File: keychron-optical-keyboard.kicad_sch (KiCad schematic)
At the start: 188 parts

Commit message: Add footprints
M  .gitignore
A  Footprints.pretty/BlackPill_STLINK.kicad_mod
M  Footprints.pretty/BlackPill_STLINK2.kicad_mod
M  Footprints.pretty/Keychron_Optical_Switch_1.25u.kicad_mod
M  Footprints.pretty/Keychron_Optical_Switch_1.5u.kicad_mod
M  Footprints.pretty/Keychron_Optical_Switch_1.75u.kicad_mod
M  Footprints.pretty/Keychron_Optical_Switch_1u.kicad_mod
M  Footprints.pretty/Keychron_Optical_Switch_2u.kicad_mod
M  MySymbols.kicad_sym
D  keychron-optical-keyboard-backups/keychron-optical-keyboard-2022-08-03_201538.zip
D  keychron-optical-keyboard-backups/keychron-optical-keyboard-2022-08-03_202112.zip
M  keychron-optical-keyboard.kicad_pcb
M  keychron-optical-keyboard.kicad_prl
M  keychron-optical-keyboard.kicad_sch
A  placek.py
A  resources/keychronpic.png
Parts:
- removed R? (x15): R, symbol Device:R
- added RP1, RP10, RP11, RP12, RP13, RP14, RP15, RP2, RP3, RP4, RP5, RP6, RP7, RP8, RP9: R_PT, Resistor_SMD:R_0805_2012Metric_Pad1.20x1.40mm_HandSolder, symbol MySymbols:R_PT
- H1, H10, H11, H12, H13, H14, H15, H16, H2, H3, H4, H5, H6, H7, H8, H9: renamed from H?; footprint (none) -> MyFootprints:MountingHole_2.2mm_M2_jlcpcb
- H17, H18, H19, H20: renamed from H?; footprint (none) -> MyFootprints:MountingHole_1.2mm_M1
- RL1, RL10, RL11, RL12, RL13, RL14, RL15, RL16, RL17, RL18, RL19, RL2, RL20, RL21, RL22, RL23, RL24, RL25, RL26, RL27, RL28, RL29, RL3, RL30, RL31, RL32, RL33, RL34, RL35, RL36, RL37, RL38, RL39, RL4, RL40, RL41, RL42, RL43, RL44, RL45, RL46, RL47, RL48, RL49, RL5, RL50, RL51, RL52, RL53, RL54, RL55, RL56, RL57, RL58, RL59, RL6, RL60, RL61, RL62, RL63, RL64, RL65, RL66, RL67, RL68, RL69, RL7, RL70, RL71, RL72, RL73, RL74, RL75, RL8, RL9: renamed from RL?; footprint (none) -> Resistor_SMD:R_1206_3216Metric_Pad1.30x1.75mm_HandSolder
- S1, S10, S11, S12, S13, S14, S15, S17, S18, S19, S2, S20, S21, S22, S23, S24, S25, S26, S27, S28, S3, S30, S31, S33, S34, S35, S36, S37, S38, S39, S4, S40, S41, S42, S43, S45, S47, S48, S49, S5, S50, S51, S52, S53, S54, S55, S56, S57, S59, S6, S60, S61, S62, S63, S64, S65, S67, S69, S7, S70, S71, S72, S73, S74, S75, S8, S9: renamed from Q?; footprint (none) -> MyFootprints:Keychron_Optical_Switch_1u
- S16, S29: renamed from Q?; footprint (none) -> MyFootprints:Keychron_Optical_Switch_1.5u
- S32, S58: renamed from Q?; footprint (none) -> MyFootprints:Keychron_Optical_Switch_1.25u
- S44, S46, S66, S68: renamed from Q?; footprint (none) -> MyFootprints:Keychron_Optical_Switch_1.75u
- U1: renamed from U?; footprint blackpill:BlackPill_STLINK -> MyFootprints:BlackPill_STLINK2
- gave numbers to parts that had none: 2
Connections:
- net 3v3: now also RP1.2, RP10.2, RP11.2, RP12.2, RP13.2, RP14.2, RP15.2, RP2.2, RP3.2, RP4.2, RP5.2, RP6.2, RP7.2, RP8.2, RP9.2
- net col1: now also RP1.1
- net col10: now also RP10.1
- net col11: now also RP11.1
- net col12: now also RP12.1
- net col13: now also RP13.1
- net col14: now also RP14.1
- net col15: now also RP15.1
- net col2: now also RP2.1
- net col3: now also RP3.1
- net col4: now also RP4.1
- net col5: now also RP5.1
- net col6: now also RP6.1
- net col7: now also RP7.1
- net col8: now also RP8.1
- net col9: now also RP9.1

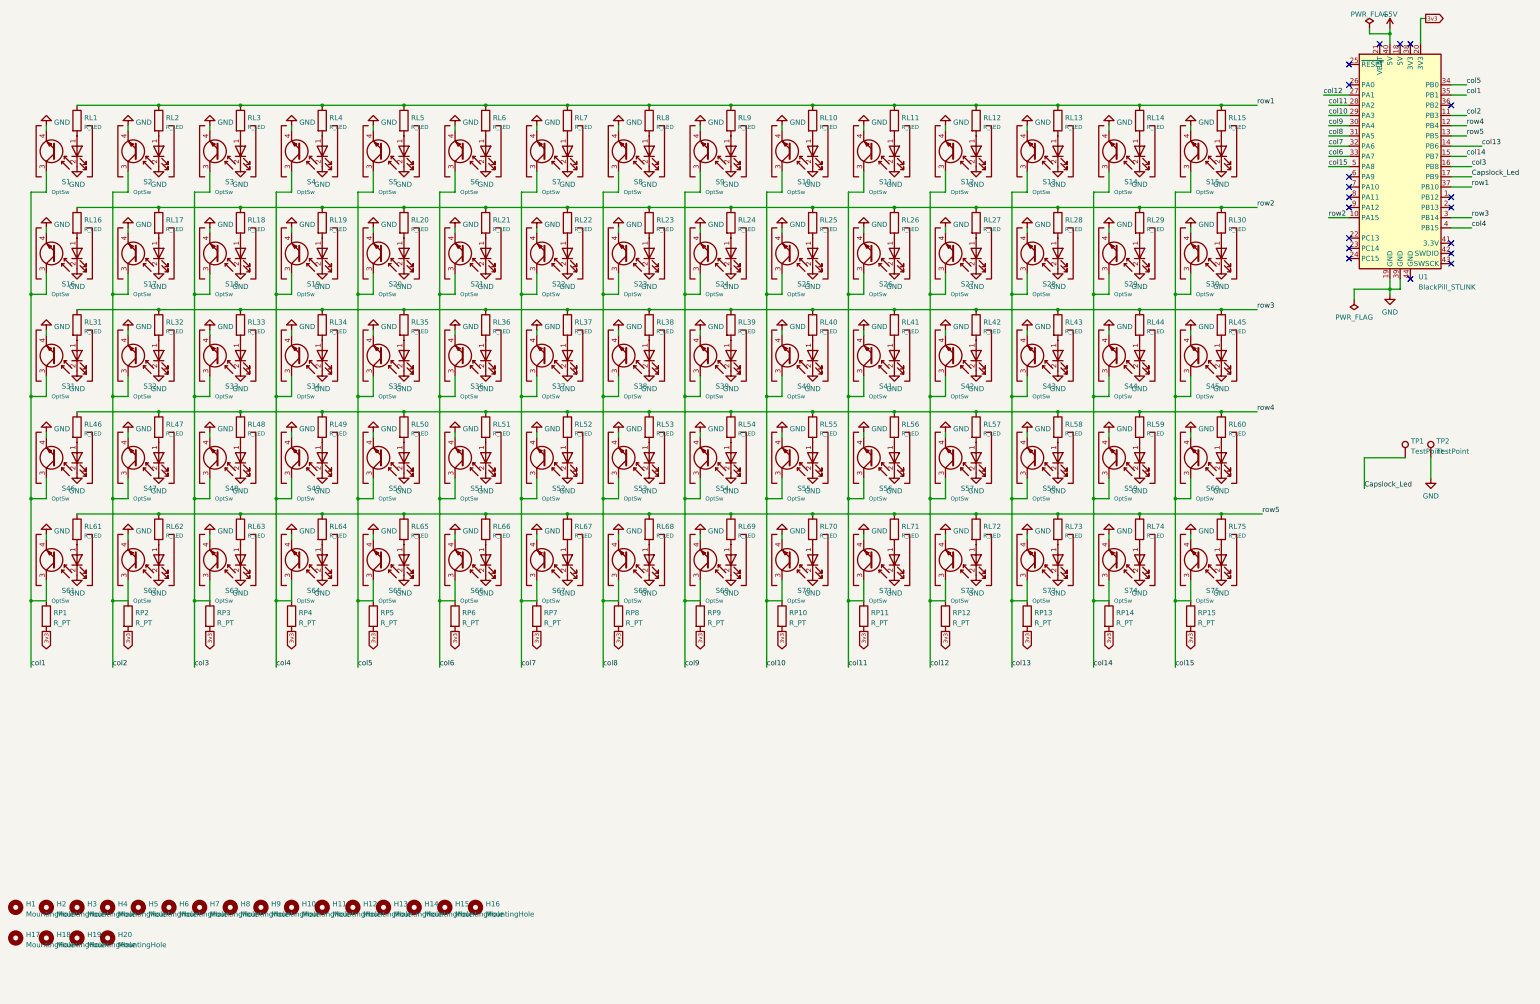
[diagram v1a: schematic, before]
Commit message: Route tracks, add switch plate, scripts
Add python scripts to route tracks, draw border, place footprints

A  Footprints.pretty/BlackPill_STLINK_Down.kicad_mod
A  Footprints.pretty/Border_PCB_WR.kicad_mod
M  Footprints.pretty/Keychron_Optical_Switch_1.25u.kicad_mod
M  Footprints.pretty/Keychron_Optical_Switch_1.5u.kicad_mod
D  Footprints.pretty/Keychron_Optical_Switch_1.75u.kicad_mod
M  Footprints.pretty/Keychron_Optical_Switch_1u.kicad_mod
D  Footprints.pretty/Keychron_Optical_Switch_2u.kicad_mod
A  Footprints.pretty/MountingHole_2.2mm_M2_ISO7380_Pad.kicad_mod
A  Footprints.pretty/SMTSO_M1.6.kicad_mod
A  Footprints.pretty/SMTSO_M2.kicad_mod
M  Footprints.pretty/Switch_Cutout.kicad_mod
M  MySymbols.kicad_sym
D  keychron-optical-keyboard-backups/keychron-optical-keyboard-2022-08-03_203051.zip
D  keychron-optical-keyboard-backups/keychron-optical-keyboard-2022-08-03_203709.zip
D  keychron-optical-keyboard-backups/keychron-optical-keyboard-2022-08-03_204429.zip
D  keychron-optical-keyboard-backups/keychron-optical-keyboard-2022-08-03_204938.zip
M  keychron-optical-keyboard.kicad_pcb
M  keychron-optical-keyboard.kicad_prl
M  keychron-optical-keyboard.kicad_sch
M  placek.py
A  resources/AL-S0602IRC-VI-12P9.pdf
A  resources/AL-S0602PTB-VI-1216.pdf
A  resources/IMG_0621.JPG
M  resources/keychronpic.png
A  switch-plate/.gitignore
A  switch-plate/fp-lib-table
A  switch-plate/switch-plate.kicad_pcb
A  switch-plate/switch-plate.kicad_prl
A  switch-plate/switch-plate.kicad_pro
A  switch-plate/switch-plate.kicad_sch
A  switch-plate/sym-lib-table
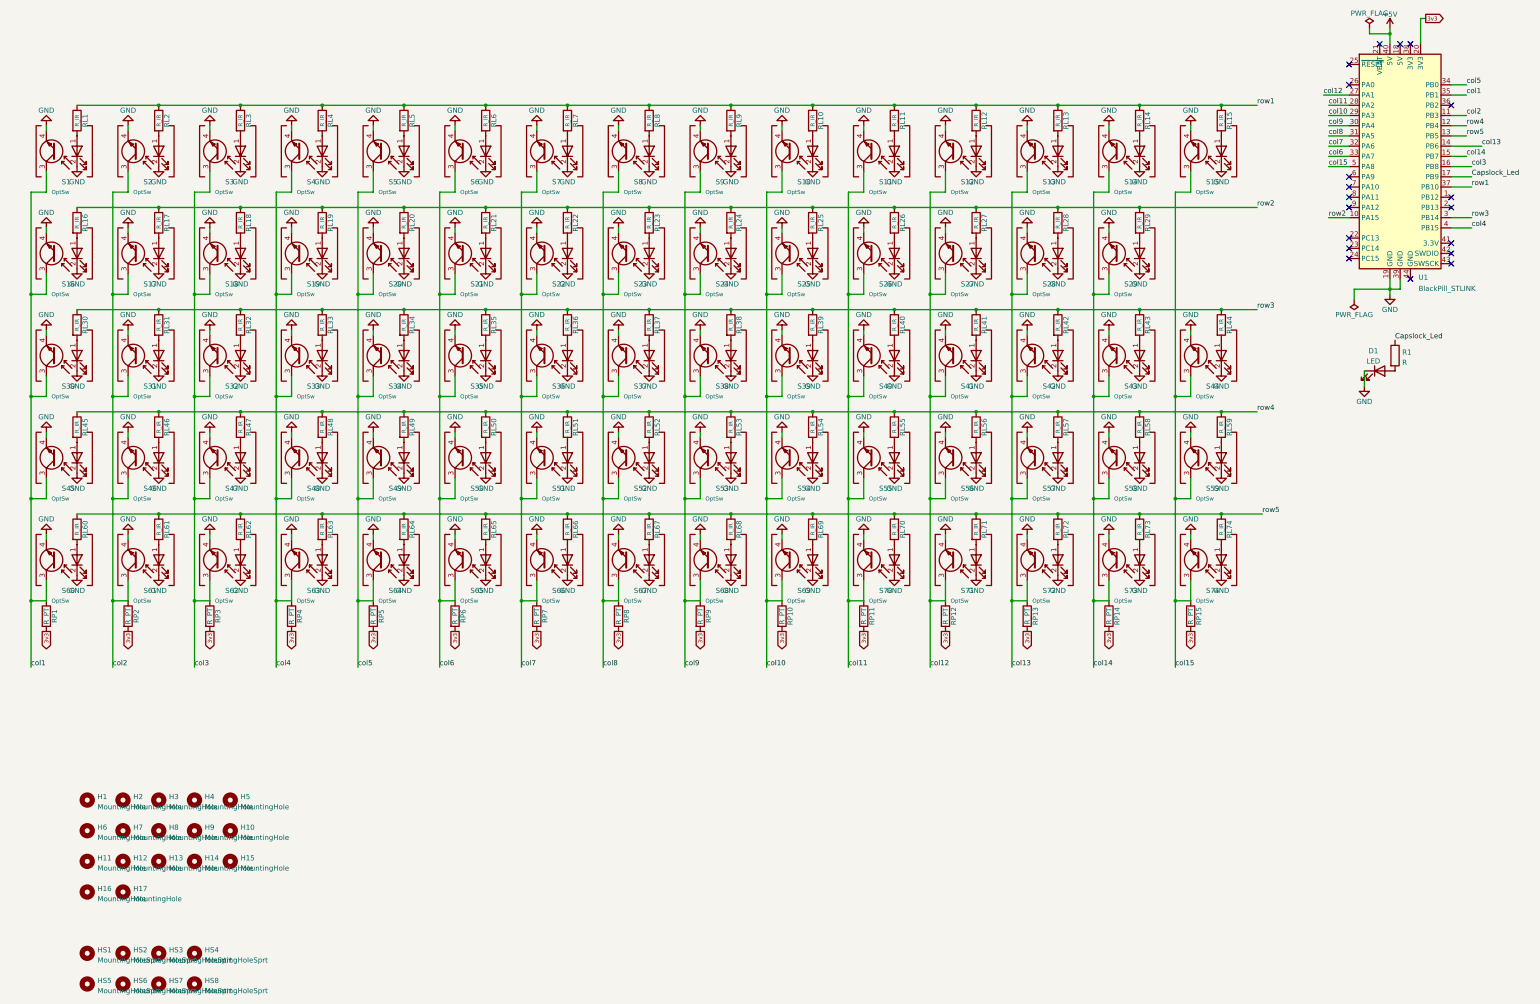
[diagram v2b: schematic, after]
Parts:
- removed H18, H19, H20: MountingHole, MyFootprints:MountingHole_1.2mm_M1, symbol Mechanical:MountingHole
- removed RL30: R_LED, Resistor_SMD:R_1206_3216Metric_Pad1.30x1.75mm_HandSolder, symbol MySymbols:R_LED
- removed S30: OptSw, MyFootprints:Keychron_Optical_Switch_1u, symbol MySymbols:OptSw
- removed TP1, TP2: TestPoint, TestPoint:TestPoint_THTPad_1.0x1.0mm_Drill0.5mm, symbol Connector:TestPoint
- added D1: LED, LED_SMD:LED_0603_1608Metric_Pad1.05x0.95mm_HandSolder, symbol Device:LED
- added HS1, HS2, HS3, HS4, HS5, HS6, HS7, HS8: MountingHoleSprt, MyFootprints:SMTSO_M2, symbol MySymbols:MountingHoleSprt
- added R1: R, Resistor_SMD:R_0805_2012Metric_Pad1.20x1.40mm_HandSolder, symbol Device:R
- H1, H10, H11, H12, H13, H14, H15, H16, H2, H3, H4, H5, H6, H7, H8, H9: footprint MyFootprints:MountingHole_2.2mm_M2_jlcpcb -> MyFootprints:SMTSO_M1.6
- H17: footprint MyFootprints:MountingHole_1.2mm_M1 -> MyFootprints:SMTSO_M1.6
- RL1: value R_LED -> R_IR; footprint Resistor_SMD:R_1206_3216Metric_Pad1.30x1.75mm_HandSolder -> Resistor_SMD:R_0805_2012Metric_Pad1.20x1.40mm_HandSolder; symbol MySymbols:R_LED -> MySymbols:R_IR; JLC 0603-1608 -> (none); LCSC C4190 -> (none)
- RL10, RL11, RL12, RL13, RL14, RL15, RL16, RL17, RL18, RL19, RL2, RL20, RL21, RL22, RL23, RL24, RL25, RL26, RL27, RL28, RL29, RL3, RL4, RL5, RL6, RL7, RL8, RL9: value R_LED -> R_IR; footprint Resistor_SMD:R_1206_3216Metric_Pad1.30x1.75mm_HandSolder -> Resistor_SMD:R_0805_2012Metric_Pad1.20x1.40mm_HandSolder; symbol MySymbols:R_LED -> MySymbols:R_IR
- RL30: renamed from RL31; value R_LED -> R_IR; footprint Resistor_SMD:R_1206_3216Metric_Pad1.30x1.75mm_HandSolder -> Resistor_SMD:R_0805_2012Metric_Pad1.20x1.40mm_HandSolder; symbol MySymbols:R_LED -> MySymbols:R_IR
- RL31: renamed from RL32; value R_LED -> R_IR; footprint Resistor_SMD:R_1206_3216Metric_Pad1.30x1.75mm_HandSolder -> Resistor_SMD:R_0805_2012Metric_Pad1.20x1.40mm_HandSolder; symbol MySymbols:R_LED -> MySymbols:R_IR
- RL32: renamed from RL33; value R_LED -> R_IR; footprint Resistor_SMD:R_1206_3216Metric_Pad1.30x1.75mm_HandSolder -> Resistor_SMD:R_0805_2012Metric_Pad1.20x1.40mm_HandSolder; symbol MySymbols:R_LED -> MySymbols:R_IR
- RL33: renamed from RL34; value R_LED -> R_IR; footprint Resistor_SMD:R_1206_3216Metric_Pad1.30x1.75mm_HandSolder -> Resistor_SMD:R_0805_2012Metric_Pad1.20x1.40mm_HandSolder; symbol MySymbols:R_LED -> MySymbols:R_IR
- RL34: renamed from RL35; value R_LED -> R_IR; footprint Resistor_SMD:R_1206_3216Metric_Pad1.30x1.75mm_HandSolder -> Resistor_SMD:R_0805_2012Metric_Pad1.20x1.40mm_HandSolder; symbol MySymbols:R_LED -> MySymbols:R_IR
- RL35: renamed from RL36; value R_LED -> R_IR; footprint Resistor_SMD:R_1206_3216Metric_Pad1.30x1.75mm_HandSolder -> Resistor_SMD:R_0805_2012Metric_Pad1.20x1.40mm_HandSolder; symbol MySymbols:R_LED -> MySymbols:R_IR
- RL36: renamed from RL37; value R_LED -> R_IR; footprint Resistor_SMD:R_1206_3216Metric_Pad1.30x1.75mm_HandSolder -> Resistor_SMD:R_0805_2012Metric_Pad1.20x1.40mm_HandSolder; symbol MySymbols:R_LED -> MySymbols:R_IR
- RL37: renamed from RL38; value R_LED -> R_IR; footprint Resistor_SMD:R_1206_3216Metric_Pad1.30x1.75mm_HandSolder -> Resistor_SMD:R_0805_2012Metric_Pad1.20x1.40mm_HandSolder; symbol MySymbols:R_LED -> MySymbols:R_IR
- RL38: renamed from RL39; value R_LED -> R_IR; footprint Resistor_SMD:R_1206_3216Metric_Pad1.30x1.75mm_HandSolder -> Resistor_SMD:R_0805_2012Metric_Pad1.20x1.40mm_HandSolder; symbol MySymbols:R_LED -> MySymbols:R_IR
- RL39: renamed from RL40; value R_LED -> R_IR; footprint Resistor_SMD:R_1206_3216Metric_Pad1.30x1.75mm_HandSolder -> Resistor_SMD:R_0805_2012Metric_Pad1.20x1.40mm_HandSolder; symbol MySymbols:R_LED -> MySymbols:R_IR
- RL40: renamed from RL41; value R_LED -> R_IR; footprint Resistor_SMD:R_1206_3216Metric_Pad1.30x1.75mm_HandSolder -> Resistor_SMD:R_0805_2012Metric_Pad1.20x1.40mm_HandSolder; symbol MySymbols:R_LED -> MySymbols:R_IR
- RL41: renamed from RL42; value R_LED -> R_IR; footprint Resistor_SMD:R_1206_3216Metric_Pad1.30x1.75mm_HandSolder -> Resistor_SMD:R_0805_2012Metric_Pad1.20x1.40mm_HandSolder; symbol MySymbols:R_LED -> MySymbols:R_IR
- RL42: renamed from RL43; value R_LED -> R_IR; footprint Resistor_SMD:R_1206_3216Metric_Pad1.30x1.75mm_HandSolder -> Resistor_SMD:R_0805_2012Metric_Pad1.20x1.40mm_HandSolder; symbol MySymbols:R_LED -> MySymbols:R_IR
- RL43: renamed from RL44; value R_LED -> R_IR; footprint Resistor_SMD:R_1206_3216Metric_Pad1.30x1.75mm_HandSolder -> Resistor_SMD:R_0805_2012Metric_Pad1.20x1.40mm_HandSolder; symbol MySymbols:R_LED -> MySymbols:R_IR
- RL44: renamed from RL45; value R_LED -> R_IR; footprint Resistor_SMD:R_1206_3216Metric_Pad1.30x1.75mm_HandSolder -> Resistor_SMD:R_0805_2012Metric_Pad1.20x1.40mm_HandSolder; symbol MySymbols:R_LED -> MySymbols:R_IR
- RL45: renamed from RL46; value R_LED -> R_IR; footprint Resistor_SMD:R_1206_3216Metric_Pad1.30x1.75mm_HandSolder -> Resistor_SMD:R_0805_2012Metric_Pad1.20x1.40mm_HandSolder; symbol MySymbols:R_LED -> MySymbols:R_IR
- RL46: renamed from RL47; value R_LED -> R_IR; footprint Resistor_SMD:R_1206_3216Metric_Pad1.30x1.75mm_HandSolder -> Resistor_SMD:R_0805_2012Metric_Pad1.20x1.40mm_HandSolder; symbol MySymbols:R_LED -> MySymbols:R_IR
- RL47: renamed from RL48; value R_LED -> R_IR; footprint Resistor_SMD:R_1206_3216Metric_Pad1.30x1.75mm_HandSolder -> Resistor_SMD:R_0805_2012Metric_Pad1.20x1.40mm_HandSolder; symbol MySymbols:R_LED -> MySymbols:R_IR
- RL48: renamed from RL49; value R_LED -> R_IR; footprint Resistor_SMD:R_1206_3216Metric_Pad1.30x1.75mm_HandSolder -> Resistor_SMD:R_0805_2012Metric_Pad1.20x1.40mm_HandSolder; symbol MySymbols:R_LED -> MySymbols:R_IR
- RL49: renamed from RL50; value R_LED -> R_IR; footprint Resistor_SMD:R_1206_3216Metric_Pad1.30x1.75mm_HandSolder -> Resistor_SMD:R_0805_2012Metric_Pad1.20x1.40mm_HandSolder; symbol MySymbols:R_LED -> MySymbols:R_IR
- RL50: renamed from RL51; value R_LED -> R_IR; footprint Resistor_SMD:R_1206_3216Metric_Pad1.30x1.75mm_HandSolder -> Resistor_SMD:R_0805_2012Metric_Pad1.20x1.40mm_HandSolder; symbol MySymbols:R_LED -> MySymbols:R_IR
- RL51: renamed from RL52; value R_LED -> R_IR; footprint Resistor_SMD:R_1206_3216Metric_Pad1.30x1.75mm_HandSolder -> Resistor_SMD:R_0805_2012Metric_Pad1.20x1.40mm_HandSolder; symbol MySymbols:R_LED -> MySymbols:R_IR
- RL52: renamed from RL53; value R_LED -> R_IR; footprint Resistor_SMD:R_1206_3216Metric_Pad1.30x1.75mm_HandSolder -> Resistor_SMD:R_0805_2012Metric_Pad1.20x1.40mm_HandSolder; symbol MySymbols:R_LED -> MySymbols:R_IR
- RL53: renamed from RL54; value R_LED -> R_IR; footprint Resistor_SMD:R_1206_3216Metric_Pad1.30x1.75mm_HandSolder -> Resistor_SMD:R_0805_2012Metric_Pad1.20x1.40mm_HandSolder; symbol MySymbols:R_LED -> MySymbols:R_IR
- RL54: renamed from RL55; value R_LED -> R_IR; footprint Resistor_SMD:R_1206_3216Metric_Pad1.30x1.75mm_HandSolder -> Resistor_SMD:R_0805_2012Metric_Pad1.20x1.40mm_HandSolder; symbol MySymbols:R_LED -> MySymbols:R_IR
- RL55: renamed from RL56; value R_LED -> R_IR; footprint Resistor_SMD:R_1206_3216Metric_Pad1.30x1.75mm_HandSolder -> Resistor_SMD:R_0805_2012Metric_Pad1.20x1.40mm_HandSolder; symbol MySymbols:R_LED -> MySymbols:R_IR
- RL56: renamed from RL57; value R_LED -> R_IR; footprint Resistor_SMD:R_1206_3216Metric_Pad1.30x1.75mm_HandSolder -> Resistor_SMD:R_0805_2012Metric_Pad1.20x1.40mm_HandSolder; symbol MySymbols:R_LED -> MySymbols:R_IR
- RL57: renamed from RL58; value R_LED -> R_IR; footprint Resistor_SMD:R_1206_3216Metric_Pad1.30x1.75mm_HandSolder -> Resistor_SMD:R_0805_2012Metric_Pad1.20x1.40mm_HandSolder; symbol MySymbols:R_LED -> MySymbols:R_IR
- RL58: renamed from RL59; value R_LED -> R_IR; footprint Resistor_SMD:R_1206_3216Metric_Pad1.30x1.75mm_HandSolder -> Resistor_SMD:R_0805_2012Metric_Pad1.20x1.40mm_HandSolder; symbol MySymbols:R_LED -> MySymbols:R_IR
- RL59: renamed from RL60; value R_LED -> R_IR; footprint Resistor_SMD:R_1206_3216Metric_Pad1.30x1.75mm_HandSolder -> Resistor_SMD:R_0805_2012Metric_Pad1.20x1.40mm_HandSolder; symbol MySymbols:R_LED -> MySymbols:R_IR
- RL60: renamed from RL61; value R_LED -> R_IR; footprint Resistor_SMD:R_1206_3216Metric_Pad1.30x1.75mm_HandSolder -> Resistor_SMD:R_0805_2012Metric_Pad1.20x1.40mm_HandSolder; symbol MySymbols:R_LED -> MySymbols:R_IR
- RL61: renamed from RL62; value R_LED -> R_IR; footprint Resistor_SMD:R_1206_3216Metric_Pad1.30x1.75mm_HandSolder -> Resistor_SMD:R_0805_2012Metric_Pad1.20x1.40mm_HandSolder; symbol MySymbols:R_LED -> MySymbols:R_IR
- RL62: renamed from RL63; value R_LED -> R_IR; footprint Resistor_SMD:R_1206_3216Metric_Pad1.30x1.75mm_HandSolder -> Resistor_SMD:R_0805_2012Metric_Pad1.20x1.40mm_HandSolder; symbol MySymbols:R_LED -> MySymbols:R_IR
- RL63: renamed from RL64; value R_LED -> R_IR; footprint Resistor_SMD:R_1206_3216Metric_Pad1.30x1.75mm_HandSolder -> Resistor_SMD:R_0805_2012Metric_Pad1.20x1.40mm_HandSolder; symbol MySymbols:R_LED -> MySymbols:R_IR
- RL64: renamed from RL65; value R_LED -> R_IR; footprint Resistor_SMD:R_1206_3216Metric_Pad1.30x1.75mm_HandSolder -> Resistor_SMD:R_0805_2012Metric_Pad1.20x1.40mm_HandSolder; symbol MySymbols:R_LED -> MySymbols:R_IR
- RL65: renamed from RL66; value R_LED -> R_IR; footprint Resistor_SMD:R_1206_3216Metric_Pad1.30x1.75mm_HandSolder -> Resistor_SMD:R_0805_2012Metric_Pad1.20x1.40mm_HandSolder; symbol MySymbols:R_LED -> MySymbols:R_IR
- RL66: renamed from RL67; value R_LED -> R_IR; footprint Resistor_SMD:R_1206_3216Metric_Pad1.30x1.75mm_HandSolder -> Resistor_SMD:R_0805_2012Metric_Pad1.20x1.40mm_HandSolder; symbol MySymbols:R_LED -> MySymbols:R_IR
- RL67: renamed from RL68; value R_LED -> R_IR; footprint Resistor_SMD:R_1206_3216Metric_Pad1.30x1.75mm_HandSolder -> Resistor_SMD:R_0805_2012Metric_Pad1.20x1.40mm_HandSolder; symbol MySymbols:R_LED -> MySymbols:R_IR
- RL68: renamed from RL69; value R_LED -> R_IR; footprint Resistor_SMD:R_1206_3216Metric_Pad1.30x1.75mm_HandSolder -> Resistor_SMD:R_0805_2012Metric_Pad1.20x1.40mm_HandSolder; symbol MySymbols:R_LED -> MySymbols:R_IR
- RL69: renamed from RL70; value R_LED -> R_IR; footprint Resistor_SMD:R_1206_3216Metric_Pad1.30x1.75mm_HandSolder -> Resistor_SMD:R_0805_2012Metric_Pad1.20x1.40mm_HandSolder; symbol MySymbols:R_LED -> MySymbols:R_IR
- RL70: renamed from RL71; value R_LED -> R_IR; footprint Resistor_SMD:R_1206_3216Metric_Pad1.30x1.75mm_HandSolder -> Resistor_SMD:R_0805_2012Metric_Pad1.20x1.40mm_HandSolder; symbol MySymbols:R_LED -> MySymbols:R_IR
- RL71: renamed from RL72; value R_LED -> R_IR; footprint Resistor_SMD:R_1206_3216Metric_Pad1.30x1.75mm_HandSolder -> Resistor_SMD:R_0805_2012Metric_Pad1.20x1.40mm_HandSolder; symbol MySymbols:R_LED -> MySymbols:R_IR
- RL72: renamed from RL73; value R_LED -> R_IR; footprint Resistor_SMD:R_1206_3216Metric_Pad1.30x1.75mm_HandSolder -> Resistor_SMD:R_0805_2012Metric_Pad1.20x1.40mm_HandSolder; symbol MySymbols:R_LED -> MySymbols:R_IR
- RL73: renamed from RL74; value R_LED -> R_IR; footprint Resistor_SMD:R_1206_3216Metric_Pad1.30x1.75mm_HandSolder -> Resistor_SMD:R_0805_2012Metric_Pad1.20x1.40mm_HandSolder; symbol MySymbols:R_LED -> MySymbols:R_IR
- RL74: renamed from RL75; value R_LED -> R_IR; footprint Resistor_SMD:R_1206_3216Metric_Pad1.30x1.75mm_HandSolder -> Resistor_SMD:R_0805_2012Metric_Pad1.20x1.40mm_HandSolder; symbol MySymbols:R_LED -> MySymbols:R_IR
- S31: renamed from S32; footprint MyFootprints:Keychron_Optical_Switch_1.25u -> MyFootprints:Keychron_Optical_Switch_1u
- S43: renamed from S44; footprint MyFootprints:Keychron_Optical_Switch_1.75u -> MyFootprints:Keychron_Optical_Switch_1.25u
- S45: renamed from S46; footprint MyFootprints:Keychron_Optical_Switch_1.75u -> MyFootprints:Keychron_Optical_Switch_1.25u
- S64: renamed from S65; footprint MyFootprints:Keychron_Optical_Switch_1u -> MyFootprints:Keychron_Optical_Switch_1.25u
- S65: renamed from S66; footprint MyFootprints:Keychron_Optical_Switch_1.75u -> MyFootprints:Keychron_Optical_Switch_1.25u
- S67: renamed from S68; footprint MyFootprints:Keychron_Optical_Switch_1.75u -> MyFootprints:Keychron_Optical_Switch_1.25u
- U1: footprint MyFootprints:BlackPill_STLINK2 -> MyFootprints:BlackPill_STLINK_Down
- renumbered S31 to S30, S33 to S32, S34 to S33, S35 to S34, S36 to S35, S37 to S36, S38 to S37, S39 to S38, S40 to S39, S41 to S40, S42 to S41, S43 to S42, S45 to S44, S47 to S46, S48 to S47, S49 to S48, S50 to S49, S51 to S50, S52 to S51, S53 to S52, S54 to S53, S55 to S54, S56 to S55, S57 to S56, S58 to S57, S59 to S58, S60 to S59, S61 to S60, S62 to S61, S63 to S62, S64 to S63, S67 to S66, S69 to S68, S70 to S69, S71 to S70, S72 to S71, S73 to S72, S74 to S73, S75 to S74
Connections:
- net Capslock_Led: now also R1.1
- net GND: now also D1.1 (K)
- new net: D1.2 (A), R1.2

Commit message: Add wrist support plate and remove 2 keys
A  Footprints.pretty/Keychron_Optical_Switch_1.75u.kicad_mod
A  drawborderk.py
M  keychron-optical-keyboard.kicad_pcb
M  keychron-optical-keyboard.kicad_prl
M  keychron-optical-keyboard.kicad_pro
M  keychron-optical-keyboard.kicad_sch
M  placek.py
M  switch-plate/switch-plate.kicad_pcb
M  switch-plate/switch-plate.kicad_sch
A  wrist-support/.gitignore
A  wrist-support/fp-lib-table
A  wrist-support/sym-lib-table
A  wrist-support/wrist-support.kicad_pcb
A  wrist-support/wrist-support.kicad_prl
A  wrist-support/wrist-support.kicad_pro
A  wrist-support/wrist-support.kicad_sch
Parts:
- removed RL59, RL74: R_IR, Resistor_SMD:R_0805_2012Metric_Pad1.20x1.40mm_HandSolder, symbol MySymbols:R_IR
- removed S59, S74: OptSw, MyFootprints:Keychron_Optical_Switch_1u, symbol MySymbols:OptSw
- S45: footprint MyFootprints:Keychron_Optical_Switch_1.25u -> MyFootprints:Keychron_Optical_Switch_1.5u
- renumbered RL60 to RL59, RL61 to RL60, RL62 to RL61, RL63 to RL62, RL64 to RL63, RL65 to RL64, RL66 to RL65, RL67 to RL66, RL68 to RL67, RL69 to RL68, RL70 to RL69, RL71 to RL70, RL72 to RL71, RL73 to RL72, S60 to S59, S61 to S60, S62 to S61, S63 to S62, S64 to S63, S65 to S64, S66 to S65, S67 to S66, S68 to S67, S69 to S68, S70 to S69, S71 to S70, S72 to S71, S73 to S72
